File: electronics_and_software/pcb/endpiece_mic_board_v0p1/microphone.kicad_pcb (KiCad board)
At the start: 2 copper layers, 7.8 x 10.4 mm, 8 parts, among them J1 PDM Mic, U1 MP23DB01HPTR

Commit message: updated files
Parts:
- G1: footprint Pauls_KiCAD_Libraries:Microhone_Graphic -> Pauls_KiCAD_Libraries:Microhone_Graphic_sml
- moved G1 10.8 mm to (150.9, 96.1)
- turned H1 to 0 degrees
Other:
- rule pad_to_mask_clearance: 0.051 -> 0
- rule via_min_drill: 0.3 -> 0.2
- rule via_min_size: 0.4 -> 0.45

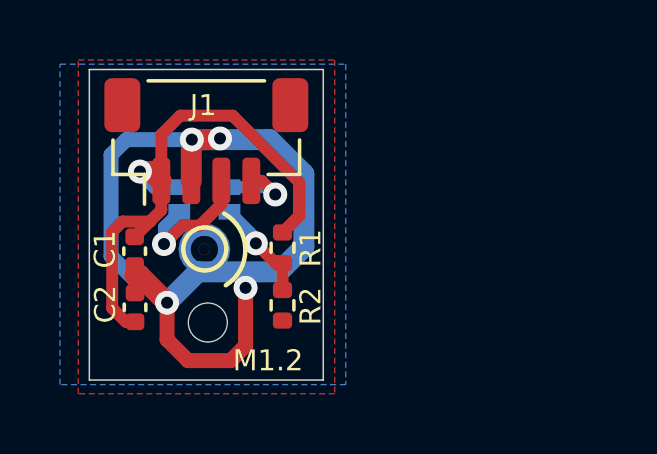
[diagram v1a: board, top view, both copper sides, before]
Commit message: Kicad V5.1 Microphone with solder connector and no screw
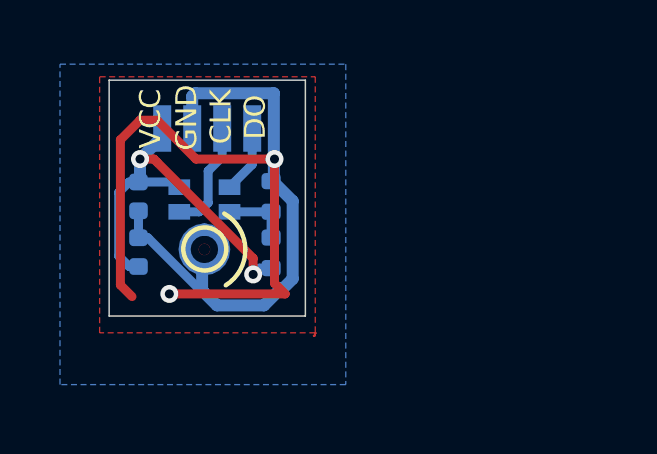
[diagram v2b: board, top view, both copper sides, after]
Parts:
- removed H1: M1.2, Pauls_KiCAD_Libraries:MountingHole_1.2mm
- C1, C2, R1, R2: moved to B.Cu
- J1: footprint Connector_JST:JST_SH_BM04B-SRSS-TB_1x04-1MP_P1.00mm_Vertical -> Pauls_KiCAD_Libraries:Solder-4P-Connector; moved to B.Cu
- moved R2 3.65 mm to (153.1, 94.4), turned to 90 degrees
- moved C2 1.85 mm to (148.7, 96.2)
- moved C1 1.83 mm to (148.7, 94.3)
- moved R1 0.42 mm to (153.1, 96.2), turned to 90 degrees
- moved J1 0.41 mm to (150.9, 92.1)
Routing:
- net GND: track 30.5 -> 38.4 mm, vias 4 -> 2
- net Net-(C1-Pad2): track 18.7 -> 13.6 mm, vias 1 -> 2
- net Net-(R1-Pad2): track 3.47 -> 2.25 mm, vias 1 -> 0
- net Net-(J1-Pad3): track 4.52 -> 3.76 mm, vias 1 -> 0
- net Net-(J1-Pad4): track 2.61 -> 2.27 mm, vias 1 -> 0
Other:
- board size 7.8 x 10.4 mm -> 6.5 x 7.9 mm
- board text added: "CLK"
- board text added: "DO"
- board text added: "GND"
- board text added: "VCC"
- board text removed: "M1.2"

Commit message: convert to kicad 6, make footprint project libs, shrink layout to smaller bord
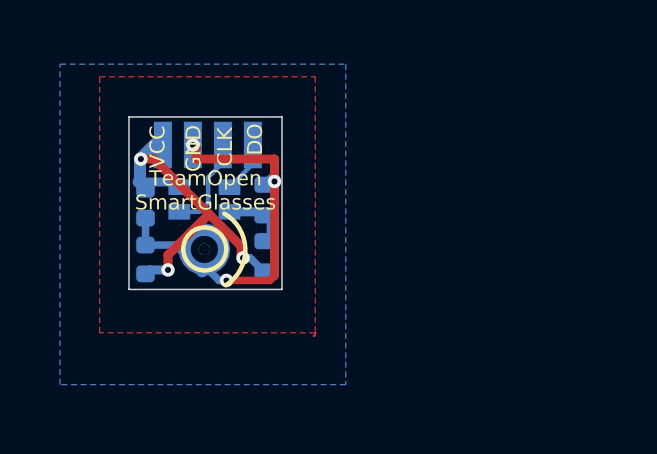
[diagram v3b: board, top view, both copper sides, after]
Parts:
- J1: footprint Pauls_KiCAD_Libraries:Solder-4P-Connector -> OSSG_footprints_endpiece:Solder-4P-Connector
- U1: value MP23DB01HPTR -> MIC; footprint Pauls_KiCAD_Libraries:MP23DB01HPTR -> OSSG_footprints_endpiece:MP23DB01HPTR
- moved J1 0.55 mm to (150.9, 92.7)
- moved C1 0.34 mm to (148.9, 94.6)
- moved C2 0.34 mm to (148.9, 96.5)
- moved R1 0.26 mm to (152.8, 96.3)
- moved R2 0.26 mm to (152.9, 94.5)
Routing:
- net GND: track 38.4 -> 13.1 mm, vias 2 -> 3
- net Net-(C1-Pad2): track 13.6 -> 13.1 mm, vias 2 -> 3
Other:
- board size 6.5 x 7.9 mm -> 5.1 x 5.8 mm
- net class Default removed
- board text added: "TeamOpen SmartGlasses"
